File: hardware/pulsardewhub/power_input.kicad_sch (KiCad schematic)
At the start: 10 parts, among them J10 XT60: 2=PLUS, 1=GND, J11 BARREL input / DNP, Q10 CSD18540Q5B, U10 LM74700QDBV

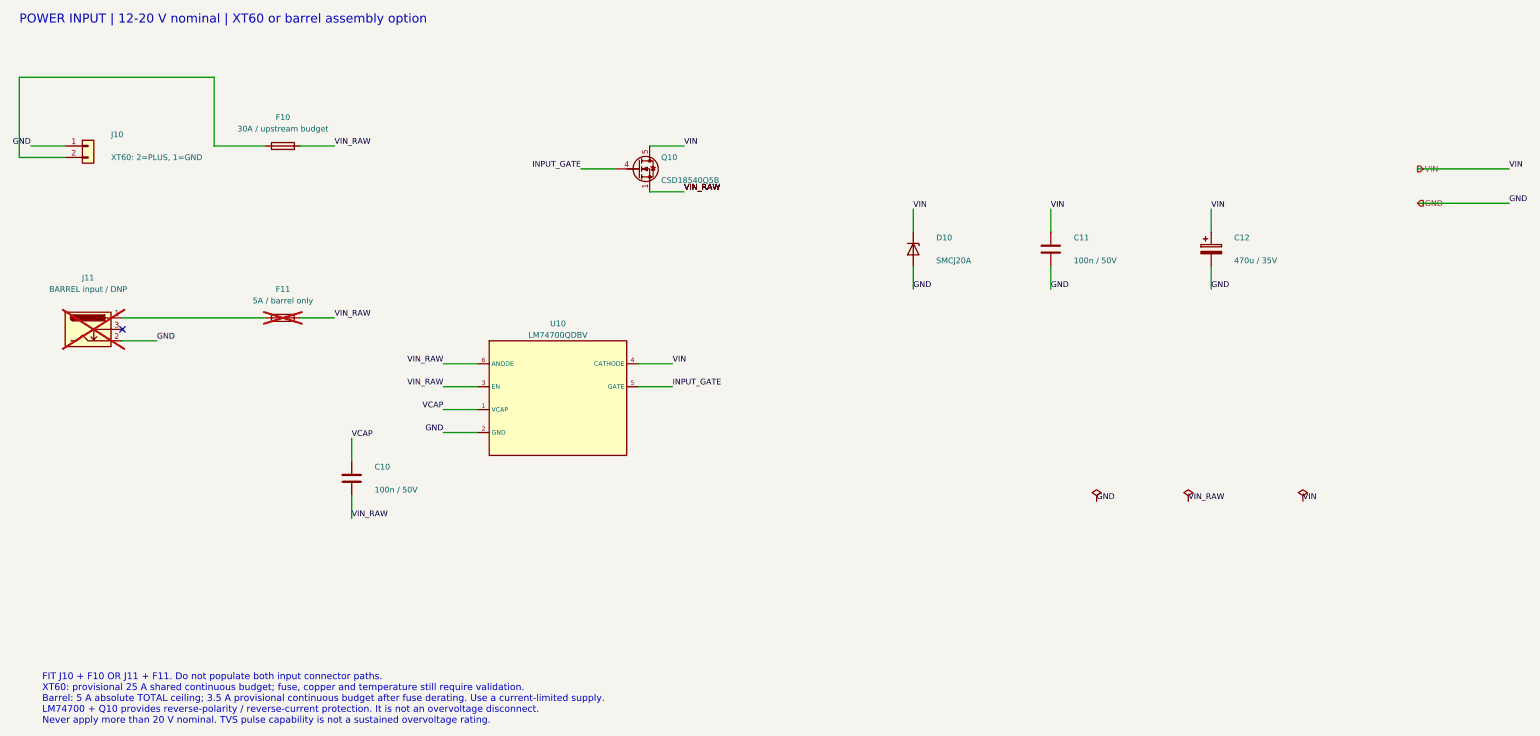
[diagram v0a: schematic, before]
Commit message: Use TPS259827 high-side switches for 12–18 V DC outlets
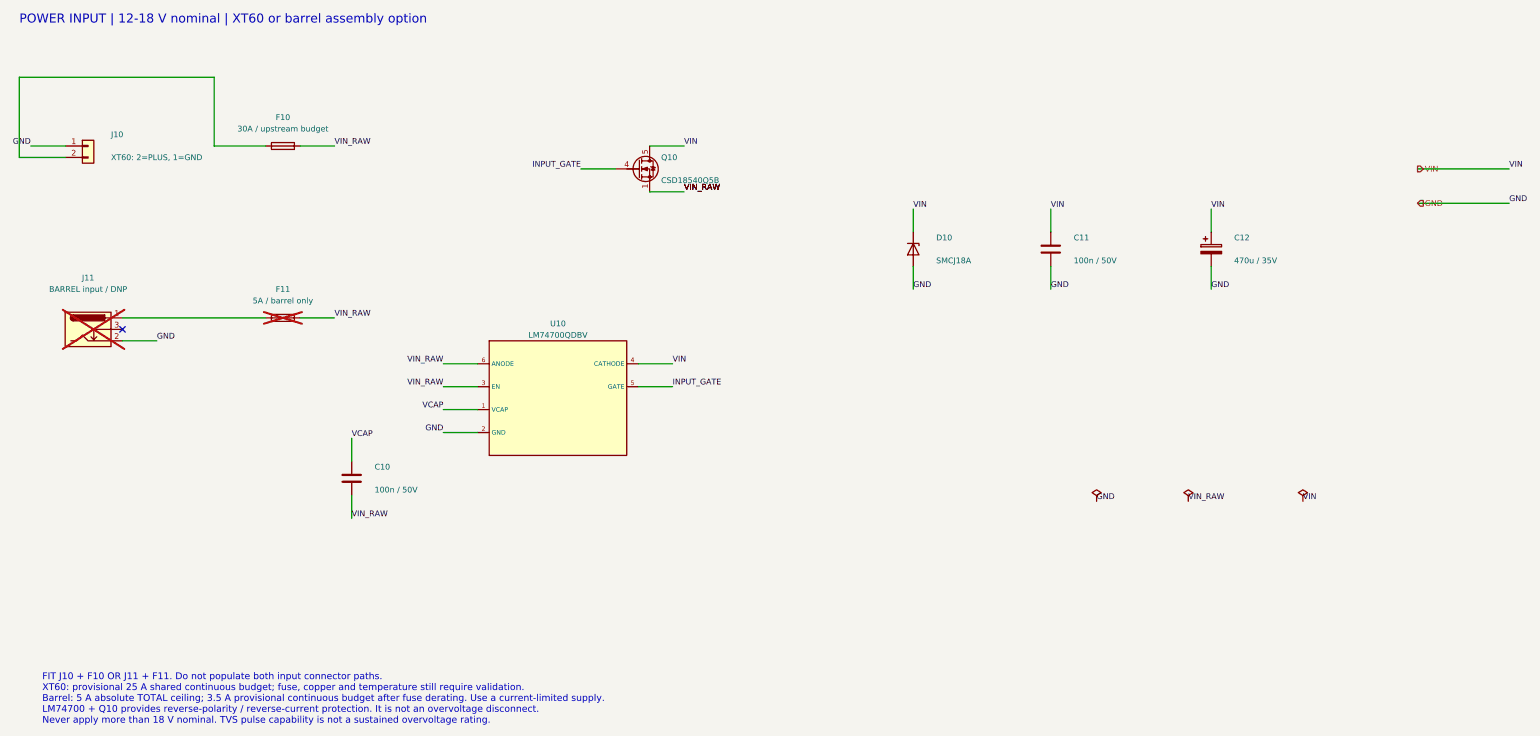
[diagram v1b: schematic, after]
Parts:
- D10: value SMCJ20A -> SMCJ18A; LCSC C2943873 -> C438102; MPN SMCJ20A -> SMCJ18A; Manufacturer GOODWORK -> Jingdao Microelectronics
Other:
- note added: "POWER INPUT | 12-18 V nominal | XT60 or barrel assembly option"
- note removed: "POWER INPUT | 12-20 V nominal | XT60 or barrel assembly option"
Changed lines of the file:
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@@
 (kicad_sch (version 20260306) (generator "eeschema") (generator_version "10.0") (paper "A3")
-(title_block (title "PulsarDew Hub - Fused input and reverse-polarity protection") (date "2026-10-03") (rev "0.1-draft") (company "PulsarFab"))
-(text "POWER INPUT | 12-20 V nominal | XT60 or barrel assembly option" (at 20.3200 16.5100 0) (effects (font (size 2 2)) (justify left top)))
+(title_block (title "PulsarDew Hub - Fused input and reverse-polarity protection") (date "2026-10-03") (rev "0.2-draft") (company "PulsarFab"))
+(text "POWER INPUT | 12-18 V nominal | XT60 or barrel assembly option" (at 20.3200 16.5100 0) (effects (font (size 2 2)) (justify left top)))
 (symbol
   (lib_id "Connector_Generic:Conn_01x02")
@@
         (size 1.27 1.27))
       (justify left)))
-  (property "Value" "SMCJ20A"
+  (property "Value" "SMCJ18A"
     (at 223.52 71.12 90.0)
     (effects
@@
         (size 1.27 1.27))
       (hide yes)))
-  (property "Datasheet" "https://datasheet.lcsc.com/datasheet/pdf/09ca1d9f88cd9aca28a35dad6b6eeb28.pdf?productCode=C2943873"
+  (property "Datasheet" "https://datasheet.lcsc.com/datasheet/pdf/30c536fe584d45c8d03dea9ed65a638b.pdf?productCode=C438102"
     (at 218.44 68.58 90.0)
     (effects
@@
         (size 1.27 1.27))
       (hide yes)))
-  (property "LCSC" "C2943873"
+  (property "LCSC" "C438102"
     (at 218.44 68.58 90.0)
     (effects
@@
         (size 1.27 1.27))
       (hide yes)))
-  (property "MPN" "SMCJ20A"
+  (property "MPN" "SMCJ18A"
     (at 218.44 68.58 90.0)
     (effects
@@
         (size 1.27 1.27))
       (hide yes)))
-  (property "Manufacturer" "GOODWORK"
+  (property "Manufacturer" "Jingdao Microelectronics"
     (at 218.44 68.58 90.0)
     (effects
@@
         (unit 1)))))
 (label "VIN"  (at 304.8000 124.4600 0) (effects (font (size 1.27 1.27)) (justify left bottom)))
-(text "FIT J10 + F10 OR J11 + F11. Do not populate both input connector paths.\nXT60: provisional 25 A shared continuous budget; fuse, copper and temperature still require validation.\nBarrel: 5 A absolute TOTAL ceiling; 3.5 A provisional continuous budget after fuse derating. Use a current-limited supply.\nLM74700 + Q10 provides reverse-polarity / reverse-current protection. It is not an overvoltage disconnect.\nNever apply more than 20 V nominal. TVS pulse capability is not a sustained overvoltage rating." (at 25.4000 162.5600 0) (effects (font (size 1.5 1.5)) (justify left top)))
+(text "FIT J10 + F10 OR J11 + F11. Do not populate both input connector paths.\nXT60: provisional 25 A shared continuous budget; fuse, copper and temperature still require validation.\nBarrel: 5 A absolute TOTAL ceiling; 3.5 A provisional continuous budget after fuse derating. Use a current-limited supply.\nLM74700 + Q10 provides reverse-polarity / reverse-current protection. It is not an overvoltage disconnect.\nNever apply more than 18 V nominal. TVS pulse capability is not a sustained overvoltage rating." (at 25.4000 162.5600 0) (effects (font (size 1.5 1.5)) (justify left top)))
 (wire (pts (xy 20.3200 30.4800) (xy 20.3200 45.7200)) (stroke (width 0) (type default)))
 (wire (pts (xy 20.3200 30.4800) (xy 63.5000 30.4800)) (stroke (width 0) (type default)))

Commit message: Reduce PulsarPower power-path cost while retaining current monitoring
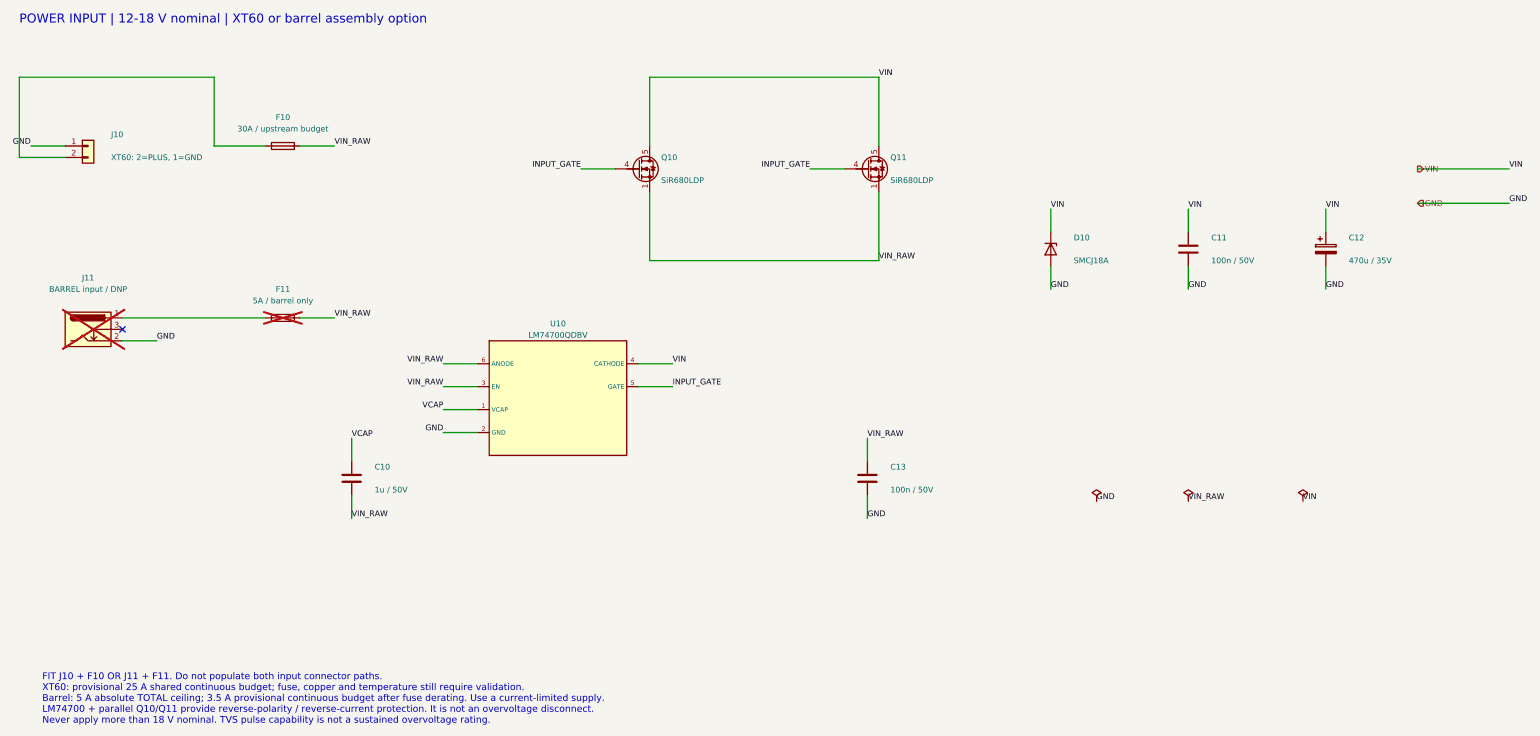
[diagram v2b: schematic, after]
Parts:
- added C13: 100n / 50V, Capacitor_SMD:C_0603_1608Metric, symbol Device:C
- added Q11: SiR680LDP, Package_SO:PowerPAK_SO-8_Single, symbol pulsarfab_hub:SiR680LDP
- C10: value 100n / 50V -> 1u / 50V; LCSC C14663 -> C15849; MPN CC0603KRX7R9BB104 -> CL10A105KB8NNNC; Manufacturer YAGEO -> Samsung Electro-Mechanics
- Q10: value CSD18540Q5B -> SiR680LDP; footprint Package_TO_SOT_SMD:TDSON-8-1 -> Package_SO:PowerPAK_SO-8_Single; symbol Transistor_FET:CSD18540Q5B -> pulsarfab_hub:SiR680LDP; LCSC C86513 -> C3279524; MPN CSD18540Q5B -> SIR680LDP-T1-RE3; Manufacturer TI -> Vishay
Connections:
- net GND: now also C13.2
- net INPUT_GATE: now also Q11.4 (G)
- net VIN: now also Q11.5 (D)
- net VIN_RAW: now also C13.1, Q11.1 (S), Q11.2 (S), Q11.3 (S)
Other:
- note added: "FIT J10 + F10 OR J11 + F11. Do not populate both input connector paths. XT60: provisional 25 A shared continuous budget; fuse, copper and temperature still require validation. Barrel: 5 A absolute TOTAL ceiling; 3.5 A provisional continuous budget after fuse derating. Use a current-limited supply. LM74700 + parallel Q10/Q11 provide reverse-polarity / reverse-current protection. It is not an overv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"
- note removed: "FIT J10 + F10 OR J11 + F11. Do not populate both input connector paths. XT60: provisional 25 A shared continuous budget; fuse, copper and temperature still require validation. Barrel: 5 A absolute TOTAL ceiling; 3.5 A provisional continuous budget after fuse derating. Use a current-limited supply. LM74700 + Q10 provides reverse-polarity / reverse-current protection. It is not an overvoltage disco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"
- title: PulsarDew Hub - Fused input and reverse-polarity protection -> PulsarPower - Fused input and reverse-polarity protection
- moved on the sheet: C11, C12, D10

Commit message: Use owned XKB barrel sockets and evaluate LMR51610 commonality
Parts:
- J11: footprint pulsarfab:BarrelJack_GCT_DCJ200_Edge -> pulsarfab:BarrelJack_XKB_DC-005K-5A_Edge; LCSC C5280493 -> C2880546; MPN DCJ200-10-A-K1-K -> DC-005K-5A-2.0; Manufacturer Global Connector Technology -> XKB Connection
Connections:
- net GND: now also J11.3
- no-connect marks 1 -> 0
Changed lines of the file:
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@@
       (font
         (size 1.27 1.27))))
-  (property "Footprint" "pulsarfab:BarrelJack_GCT_DCJ200_Edge"
+  (property "Footprint" "pulsarfab:BarrelJack_XKB_DC-005K-5A_Edge"
     (at 35.56 86.36 0.0)
     (effects
@@
         (size 1.27 1.27))
       (hide yes)))
-  (property "Datasheet" "https://datasheet.lcsc.com/datasheet/pdf/9e28732f65d9d59bee76802895b2add9.pdf?productCode=C5280493"
+  (property "Datasheet" "https://datasheet.lcsc.com/datasheet/pdf/42a925a8542473f46554cf6f67b6cc91.pdf?productCode=C2880546"
     (at 35.56 86.36 0.0)
     (effects
@@
         (size 1.27 1.27))
       (hide yes)))
-  (property "LCSC" "C5280493"
+  (property "LCSC" "C2880546"
     (at 35.56 86.36 0.0)
     (effects
@@
         (size 1.27 1.27))
       (hide yes)))
-  (property "MPN" "DCJ200-10-A-K1-K"
+  (property "MPN" "DC-005K-5A-2.0"
     (at 35.56 86.36 0.0)
     (effects
@@
         (size 1.27 1.27))
       (hide yes)))
-  (property "Manufacturer" "Global Connector Technology"
+  (property "Manufacturer" "XKB Connection"
     (at 35.56 86.36 0.0)
     (effects
@@
 (label "GND"  (at 22.8600 45.7200 180) (effects (font (size 1.27 1.27)) (justify right bottom)))
 (label "GND"  (at 50.8000 88.9000 0) (effects (font (size 1.27 1.27)) (justify left bottom)))
-(no_connect (at 43.1800 86.3600))
+(label "GND"  (at 50.8000 86.3600 0) (effects (font (size 1.27 1.27)) (justify left bottom)))
 (label "VIN_RAW"  (at 90.1700 45.7200 0) (effects (font (size 1.27 1.27)) (justify left bottom)))
 (label "VIN_RAW"  (at 90.1700 83.8200 0) (effects (font (size 1.27 1.27)) (justify left bottom)))
@@
 (wire (pts (xy 22.8600 45.7200) (xy 30.4800 45.7200)) (stroke (width 0) (type default)))
 (wire (pts (xy 43.1800 83.8200) (xy 74.9300 83.8200)) (stroke (width 0) (type default)))
+(wire (pts (xy 43.1800 86.3600) (xy 50.8000 86.3600)) (stroke (width 0) (type default)))
 (wire (pts (xy 43.1800 88.9000) (xy 50.8000 88.9000)) (stroke (width 0) (type default)))
 (wire (pts (xy 63.5000 30.4800) (xy 63.5000 45.7200)) (stroke (width 0) (type default)))
